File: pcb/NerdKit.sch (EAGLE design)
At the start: 31 parts, among them U2 ARDUINOR3-PINSONLY

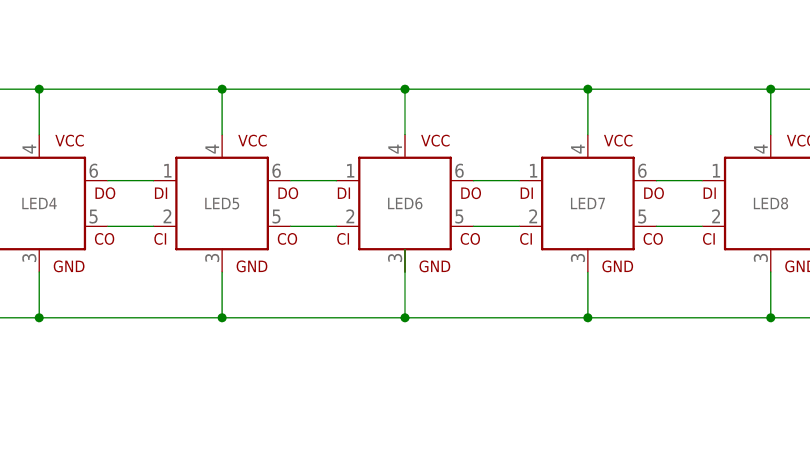
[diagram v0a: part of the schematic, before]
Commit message: Corrected schematic error on LED6 ground pin and adjusted copper pour.
Fixes #7.
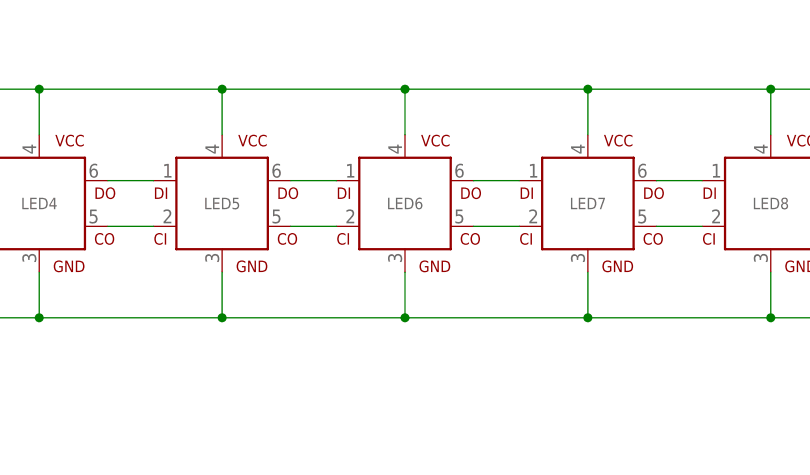
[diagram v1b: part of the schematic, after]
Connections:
- net GND: now also LED6.GND
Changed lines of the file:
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@@
 <pinref part="SUPPLY3" gate="GND" pin="GND"/>
 <wire x1="99.06" y1="-63.5" x2="99.06" y2="-58.42" width="0.1524" layer="91"/>
+<junction x="139.7" y="-58.42"/>
+<pinref part="LED7" gate="G$1" pin="GND"/>
 <wire x1="139.7" y1="-58.42" x2="160.02" y2="-58.42" width="0.1524" layer="91"/>
-<junction x="139.7" y="-58.42"/>
-<wire x1="160.02" y1="-50.8" x2="160.02" y2="-58.42" width="0.1524" layer="91"/>
-<pinref part="LED7" gate="G$1" pin="GND"/>
 <wire x1="160.02" y1="-58.42" x2="180.34" y2="-58.42" width="0.1524" layer="91"/>
 <wire x1="180.34" y1="-58.42" x2="180.34" y2="-53.34" width="0.1524" layer="91"/>
-<junction x="160.02" y="-58.42"/>
 <pinref part="LED8" gate="G$1" pin="GND"/>
 <wire x1="180.34" y1="-58.42" x2="200.66" y2="-58.42" width="0.1524" layer="91"/>
@@
 <wire x1="241.3" y1="-58.42" x2="241.3" y2="-53.34" width="0.1524" layer="91"/>
 <junction x="220.98" y="-58.42"/>
+<pinref part="LED6" gate="G$1" pin="GND"/>
+<wire x1="160.02" y1="-53.34" x2="160.02" y2="-58.42" width="0.1524" layer="91"/>
+<junction x="160.02" y="-58.42"/>
 </segment>
 <segment>

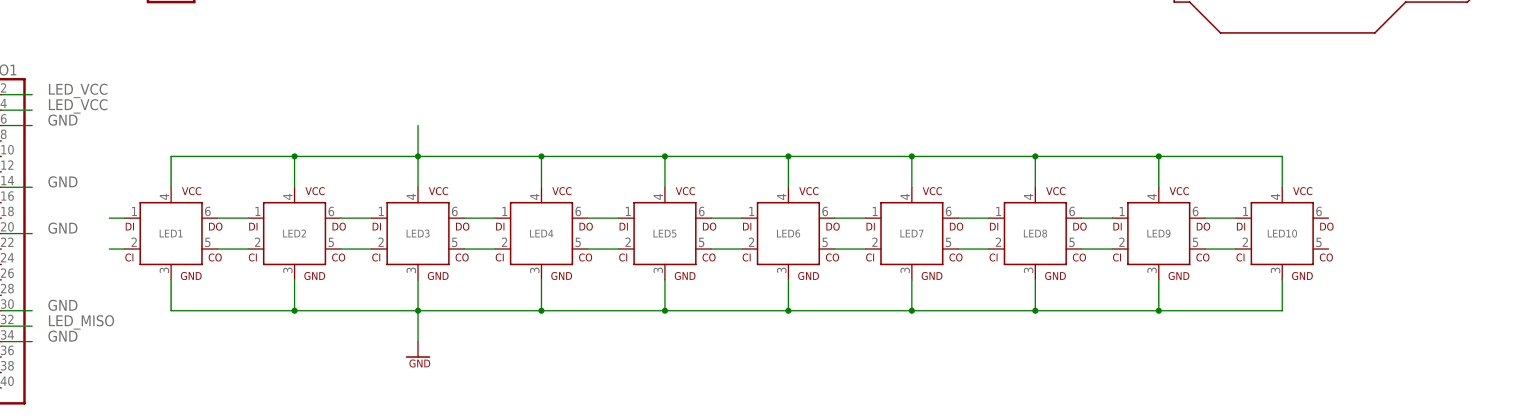
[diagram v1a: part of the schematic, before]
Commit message: Added OSH Park compliant cutouts for daughter cards.
See http://docs.oshpark.com/submitting-orders/cutouts-and-slots/.
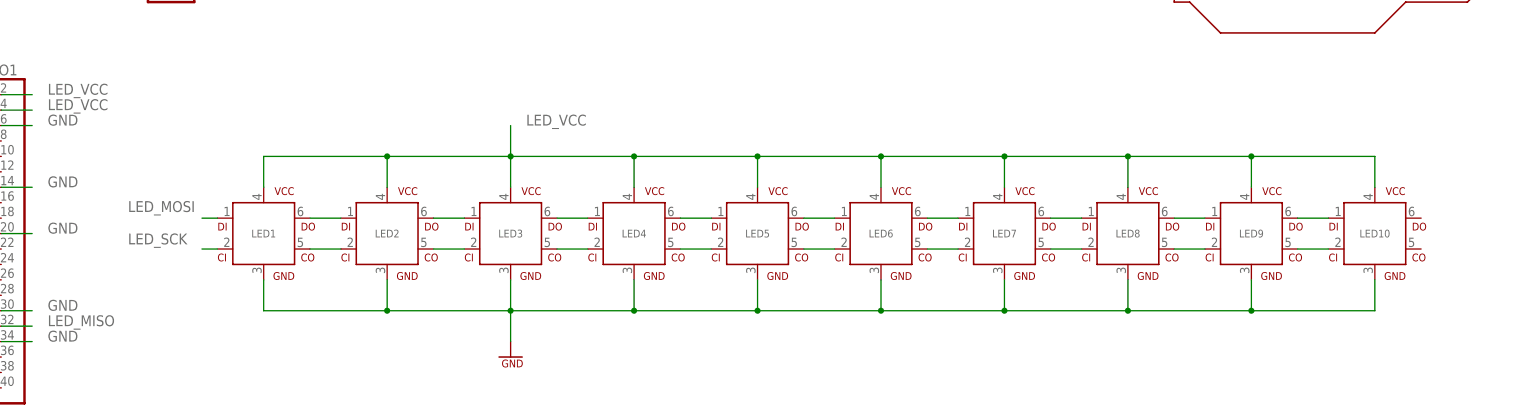
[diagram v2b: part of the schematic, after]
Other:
- moved on the sheet: LED1, LED10, LED2, LED3, LED4, LED5, LED6, LED7, LED8, LED9

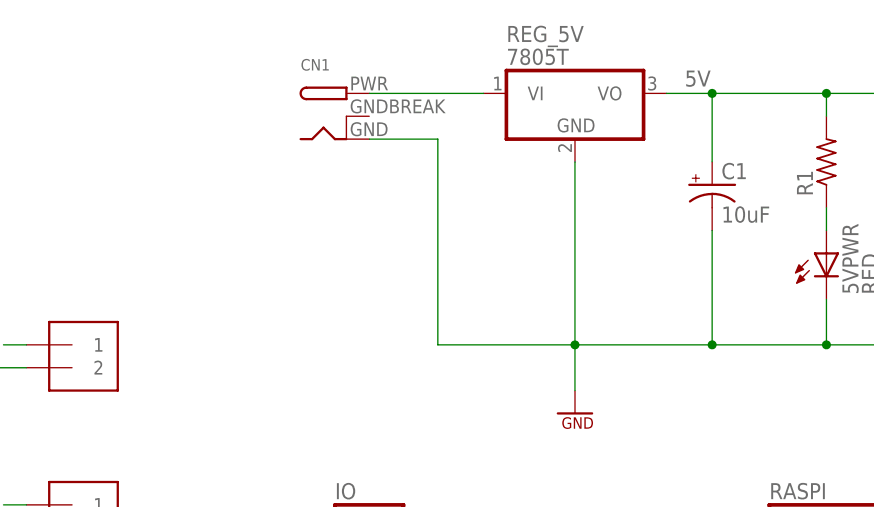
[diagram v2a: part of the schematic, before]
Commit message: Ditched the 2.1mm DC jack and regulator in favor of micro USB for power.
This fixes #5.
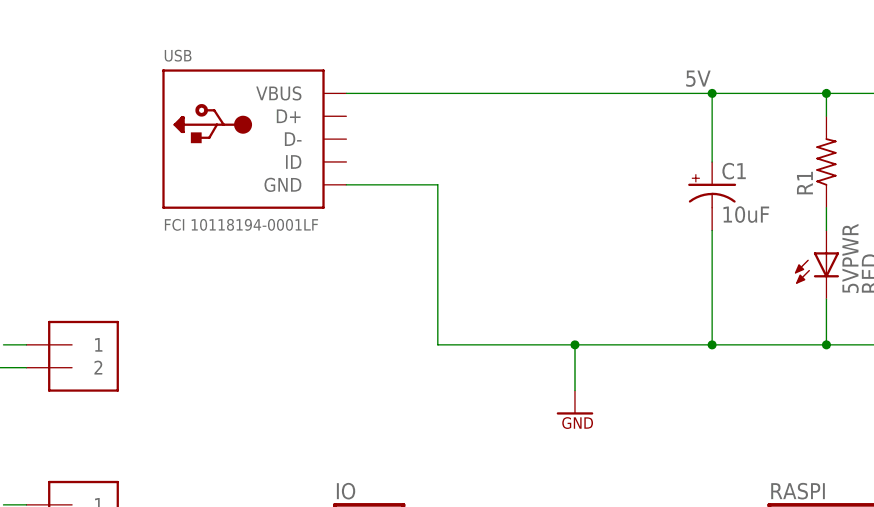
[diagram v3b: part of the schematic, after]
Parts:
- removed CN1: (no value), adafruit:DCBARRELPTH
- removed REG_5V: 7805T, adafruit:7805T
- added USB: FCI 10118194-0001LF, microbuilder:USBMICRO_20329
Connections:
- removed net N$2: CN1.PWR, REG_5V.VI
- net 5V: now also USB.VBUS; no longer REG_5V.VO
- net GND: now also USB.GND; no longer CN1.GND, REG_5V.GND
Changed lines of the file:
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@@
 <layer number="56" name="wert" color="7" fill="1" visible="no" active="no"/>
 <layer number="57" name="tCAD" color="7" fill="1" visible="no" active="no"/>
+<layer number="59" name="tCarbon" color="7" fill="1" visible="no" active="no"/>
+<layer number="60" name="bCarbon" color="7" fill="1" visible="no" active="no"/>
 <layer number="90" name="Modules" color="5" fill="1" visible="yes" active="yes"/>
 <layer number="91" name="Nets" color="2" fill="1" visible="yes" active="yes"/>
@@
 <layer number="127" name="_tValues" color="7" fill="1" visible="yes" active="yes"/>
 <layer number="128" name="_bValues" color="7" fill="1" visible="yes" active="yes"/>
+<layer number="129" name="Mask" color="7" fill="1" visible="yes" active="yes"/>
 <layer number="131" name="tAdjust" color="7" fill="1" visible="no" active="yes"/>
 <layer number="132" name="bAdjust" color="7" fill="1" visible="no" active="yes"/>
@@
 <layer number="223" name="223bmp" color="24" fill="1" visible="no" active="no"/>
 <layer number="224" name="224bmp" color="25" fill="1" visible="no" active="no"/>
+<layer number="225" name="225bmp" color="7" fill="1" visible="yes" active="yes"/>
+<layer number="226" name="226bmp" color="7" fill="1" visible="yes" active="yes"/>
+<layer number="227" name="227bmp" color="7" fill="1" visible="yes" active="yes"/>
+<layer number="228" name="228bmp" color="7" fill="1" visible="yes" active="yes"/>
+<layer number="229" name="229bmp" color="7" fill="1" visible="yes" active="yes"/>
+<layer number="230" name="230bmp" color="7" fill="1" visible="yes" active="yes"/>
 <layer number="231" name="Eagle3D_PG1" color="7" fill="1" visible="no" active="no"/>
 <layer number="232" name="Eagle3D_PG2" color="7" fill="1" visible="no" active="no"/>
@@
 <layer number="251" name="SMDround" color="7" fill="1" visible="no" active="no"/>
 <layer number="254" name="cooling" color="7" fill="1" visible="yes" active="yes"/>
+<layer number="255" name="routoute" color="7" fill="1" visible="yes" active="yes"/>
 </layers>
 <schematic xreflabel="%F%N/%S.%C%R" xrefpart="/%S.%C%R">
@@
 <part name="PB2_TB_3V3" library="adafruit" deviceset="1X2" device="-3.5MM"/>
 <part name="SUPPLY1" library="eagle-book" deviceset="GND" device=""/>
-<part name="REG_5V" library="adafruit" deviceset="78*" device="T" technology="05"/>
 <part name="REG_3V3" library="adafruit" deviceset="78*" device="L" technology="08" value="L4931"/>
 <part name="SUPPLY6" library="eagle-book" deviceset="GND" device=""/>
 <part name="C1" library="adafruit" deviceset="CPOL-US" device="E1.8-4" value="10uF"/>
 <part name="C2" library="adafruit" deviceset="CPOL-US" device="E1.8-4" value="10uF"/>
-<part name="CN1" library="adafruit" deviceset="DCBARREL" device="PTH"/>
 <part name="5VPWR" library="adafruit" deviceset="LED" device="3MM" value="RED"/>
 <part name="3V3PWR" library="adafruit" deviceset="LED" device="3MM" value="RED"/>
@@
 <part name="LED10" library="osborn" deviceset="RGBLED" device="5050"/>
 <part name="ARDUINOIO1" library="pinhead" deviceset="PINHD-2X20" device=""/>
+<part name="USB" library="microbuilder" deviceset="USB" device="MICRO_20329" value="FCI 10118194-0001LF"/>
 </parts>
 <sheets>
@@
 <instance part="PB2_TB_3V3" gate="G$1" x="25.4" y="17.78"/>
 <instance part="SUPPLY1" gate="GND" x="81.28" y="60.96"/>
-<instance part="REG_5V" gate="A1" x="81.28" y="96.52"/>
 <instance part="REG_3V3" gate="A1" x="127" y="96.52"/>
 <instance part="SUPPLY6" gate="GND" x="7.62" y="12.7"/>
 <instance part="C1" gate="G$1" x="96.52" y="86.36"/>
 <instance part="C2" gate="G$1" x="142.24" y="86.36"/>
-<instance part="CN1" gate="G$1" x="55.88" y="93.98"/>
 <instance part="5VPWR" gate="G$1" x="109.22" y="78.74"/>
 <instance part="3V3PWR" gate="G$1" x="154.94" y="78.74"/>
@@
 <instance part="LED10" gate="G$1" x="256.54" y="-45.72"/>
 <instance part="ARDUINOIO1" gate="A" x="25.4" y="-45.72"/>
+<instance part="USB" gate="G$1" x="45.72" y="91.44"/>
 </instances>
 <busses>
@@
 <net name="5V" class="0">
 <segment>
-<pinref part="REG_5V" gate="A1" pin="VO"/>
 <pinref part="REG_3V3" gate="A1" pin="VI"/>
 <label x="93.472" y="97.282" size="1.778" layer="95"/>
-<wire x1="91.44" y1="96.52" x2="96.52" y2="96.52" width="0.1524" layer="91"/>
 <wire x1="96.52" y1="96.52" x2="109.22" y2="96.52" width="0.1524" layer="91"/>
 <wire x1="109.22" y1="96.52" x2="116.84" y2="96.52" width="0.1524" layer="91"/>
@@
 <wire x1="96.52" y1="88.9" x2="96.52" y2="96.52" width="0.1524" layer="91"/>
 <junction x="96.52" y="96.52"/>
+<pinref part="USB" gate="G$1" pin="VBUS"/>
+<wire x1="55.88" y1="96.52" x2="96.52" y2="96.52" width="0.1524" layer="91"/>
 </segment>
 <segment>
@@
 <net name="GND" class="0">
 <segment>
-<pinref part="REG_5V" gate="A1" pin="GND"/>
 <pinref part="SUPPLY1" gate="GND" pin="GND"/>
 <pinref part="REG_3V3" gate="A1" pin="GND"/>
-<wire x1="81.28" y1="88.9" x2="81.28" y2="68.58" width="0.1524" layer="91"/>
 <wire x1="81.28" y1="68.58" x2="81.28" y2="63.5" width="0.1524" layer="91"/>
 <wire x1="66.04" y1="68.58" x2="81.28" y2="68.58" width="0.1524" layer="91"/>
@@
 <wire x1="109.22" y1="68.58" x2="96.52" y2="68.58" width="0.1524" layer="91"/>
 <wire x1="96.52" y1="68.58" x2="81.28" y2="68.58" width="0.1524" layer="91"/>
-<wire x1="66.04" y1="68.58" x2="66.04" y2="91.44" width="0.1524" layer="91"/>
-<pinref part="CN1" gate="G$1" pin="GND"/>
-<wire x1="66.04" y1="91.44" x2="58.42" y2="91.44" width="0.1524" layer="91"/>
+<wire x1="66.04" y1="68.58" x2="66.04" y2="86.36" width="0.1524" layer="91"/>
 <pinref part="3V3PWR" gate="G$1" pin="C"/>
 <wire x1="154.94" y1="73.66" x2="154.94" y2="68.58" width="0.1524" layer="91"/>
@@
 <wire x1="96.52" y1="81.28" x2="96.52" y2="68.58" width="0.1524" layer="91"/>
 <junction x="96.52" y="68.58"/>
+<pinref part="USB" gate="G$1" pin="GND"/>
+<wire x1="55.88" y1="86.36" x2="66.04" y2="86.36" width="0.1524" layer="91"/>
 </segment>
 <segment>
@@
 </segment>
 </net>
-<net name="N$2" class="0">
-<segment>
-<pinref part="REG_5V" gate="A1" pin="VI"/>
-<pinref part="CN1" gate="G$1" pin="PWR"/>
-<wire x1="58.42" y1="96.52" x2="71.12" y2="96.52" width="0.1524" layer="91"/>
-</segment>
-</net>
